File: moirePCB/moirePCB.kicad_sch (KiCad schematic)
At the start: 55 parts, among them J1 USB_C_Receptacle, U1 ESP32-PICO-D4, U1 TLC555xD, U10 TLV73333PDBV, U2 BQ25504, U3 TLV73333PDBV, U4 RFM95W-915S2, U5 CH340E, U7 HDC1080, U8 AP2281-1WG-7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

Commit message: Daughter Board changes from meeting
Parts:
- removed ACC_RAIL_JP1, BATTMEASURE_JP1, LDO_JP1, TEMP_SCL_JP1, TEMP_SDA_JP1, VBAT_OK1: SolderJumper_2_Bridged, Jumper:SolderJumper-2_P1.3mm_Bridged_RoundedPad1.0x1.5mm, symbol Jumper:SolderJumper_2_Bridged
- removed AE1: T1-915M Antenna, Connector_PinHeader_2.54mm:PinHeader_1x01_P2.54mm_Vertical, symbol Device:Antenna
- removed BOOT1, EN1: SW_Push, Button_Switch_SMD:SW_Push_1P1T_XKB_TS-1187A, symbol Switch:SW_Push
- removed BT1: Battery_Cell, Connector_JST:JST_PH_S2B-PH-K_1x02_P2.00mm_Horizontal, symbol Device:Battery_Cell
- removed C1: .1u, Capacitor_SMD:C_0805_2012Metric, symbol Device:C
- removed C2, C6: 12pF/50V, Capacitor_SMD:C_0805_2012Metric, symbol Device:C
- removed C3: .01uF, Capacitor_SMD:C_0805_2012Metric, symbol Device:C
- removed C5: 10u, Capacitor_SMD:C_0805_2012Metric, symbol Device:C
- removed C7: 100nF, Capacitor_SMD:C_0805_2012Metric, symbol Device:C
- removed C_FLTR1: .1uF, Capacitor_SMD:C_0805_2012Metric, symbol Device:C
- removed C_HVR1, C_STOR1: 4.7uF, Capacitor_SMD:C_0805_2012Metric, symbol Device:C
- removed J1: USB_C_Receptacle, Connector_USB:USB_C_Receptacle_HRO_TYPE-C-31-M-12, symbol Connector:USB_C_Receptacle
- removed LDR1: R_Photo 50k-100k, Connector_PinHeader_2.54mm:PinHeader_1x02_P2.54mm_Horizontal, symbol Device:R_Photo
- removed L_BST1: 22uH, Inductor_SMD:L_0805_2012Metric, symbol Device:L
- removed R10: 360k, Resistor_SMD:R_0805_2012Metric, symbol Device:R
- removed R4: 270k, Resistor_SMD:R_0805_2012Metric, symbol Device:R
- removed R6: 5.1k, Resistor_SMD:R_0805_2012Metric, symbol Device:R
- removed R7: 820k, Resistor_SMD:R_0805_2012Metric, symbol Device:R
- removed R_OC+10: 10M, Resistor_SMD:R_0805_2012Metric, symbol Device:R
- removed R_OC_1: 5.76M, Resistor_SMD:R_0805_2012Metric, symbol Device:R
- removed R_OC_2: 4.12M, Resistor_SMD:R_0805_2012Metric, symbol Device:R
- removed R_OK_1: 3.57M, Resistor_SMD:R_0805_2012Metric, symbol Device:R
- removed R_OK_2, R_UV_2: 6.19M, Resistor_SMD:R_0805_2012Metric, symbol Device:R
- removed R_OK_3: .143M, Resistor_SMD:R_0805_2012Metric, symbol Device:R
- removed R_OV_1: 4.42M, Resistor_SMD:R_0805_2012Metric, symbol Device:R
- removed R_OV_2: 5.36M, Resistor_SMD:R_0805_2012Metric, symbol Device:R
- removed R_UV_1: 3.74M, Resistor_SMD:R_0805_2012Metric, symbol Device:R
- removed SC1: Solar_Cell, Connector_PinHeader_2.54mm:PinHeader_1x02_P2.54mm_Horizontal, symbol Device:Solar_Cell
- removed U1: ESP32-PICO-D4, Package_DFN_QFN:QFN-48-1EP_7x7mm_P0.5mm_EP5.3x5.3mm, symbol RF_Module:ESP32-PICO-D4
- removed U10, U3: TLV73333PDBV, Package_TO_SOT_SMD:SOT-23-5, symbol Regulator_Linear:TLV73333PDBV
- removed U2: BQ25504, Package_DFN_QFN:VQFN-16-1EP_3x3mm_P0.5mm_EP1.68x1.68mm, symbol Battery_Management:BQ25504
- removed U4: RFM95W-915S2, RF_Module:HOPERF_RFM9XW_SMD, symbol RF_Module:RFM95W-915S2
- removed U5: CH340E, Package_SO:MSOP-10_3x3mm_P0.5mm, symbol Interface_USB:CH340E
- removed U8, U9: AP2281-1WG-7, Package_TO_SOT_SMD:SOT-23-6, symbol Power_Management:AP2281-1WG-7
- removed USB//OFF1, USB//SOLAR1: SW_DPDT_x2, Button_Switch_SMD:SW_SPDT_PCM12, symbol Switch:SW_DPDT_x2
- removed Y2: 32.768kHz, Crystal:Crystal_SMD_MicroCrystal_CM9V-T1A-2Pin_1.6x1.0mm, symbol Device:Crystal
- added J1, J2: Conn_01x13, Connector_PinHeader_2.54mm:PinHeader_1x13_P2.54mm_Vertical, symbol Connector_Generic:Conn_01x13
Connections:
- net A_VCC: now also J2.1 (Pin_1)
- net GND: now also J1.2 (Pin_2), J2.2 (Pin_2)
- net at U7.1 (SDA): now also J2.5 (Pin_5)
- net at U7.6 (SCL): now also J2.4 (Pin_4)
- new net 5V (USB): J1.1 (Pin_1)
- no-connect marks 16 -> 0
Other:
- note removed: "Accessory Rail"
- note removed: "For internal flash use"
- note removed: "Light Sensor"
- note removed: "USB/UART Converter"
- note removed: "external RTC crystal"
- note removed: "reset button"
- moved on the sheet: C1, C2, FREQOUT_JP1, R1, R2, U1, U7

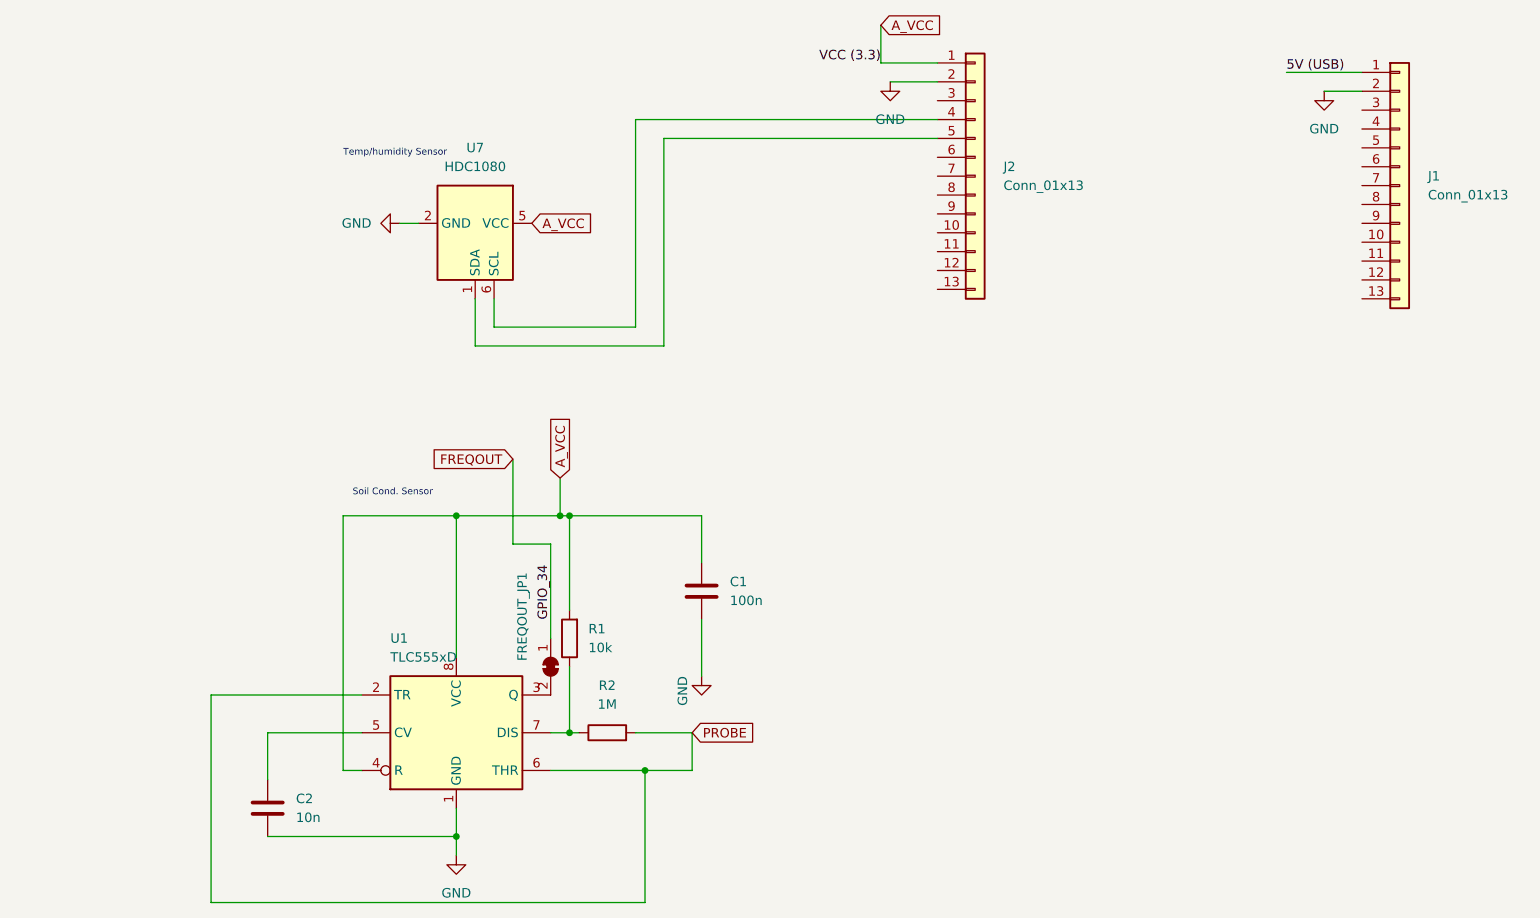
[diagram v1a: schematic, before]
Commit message: Daughter board prototype 1.0.0
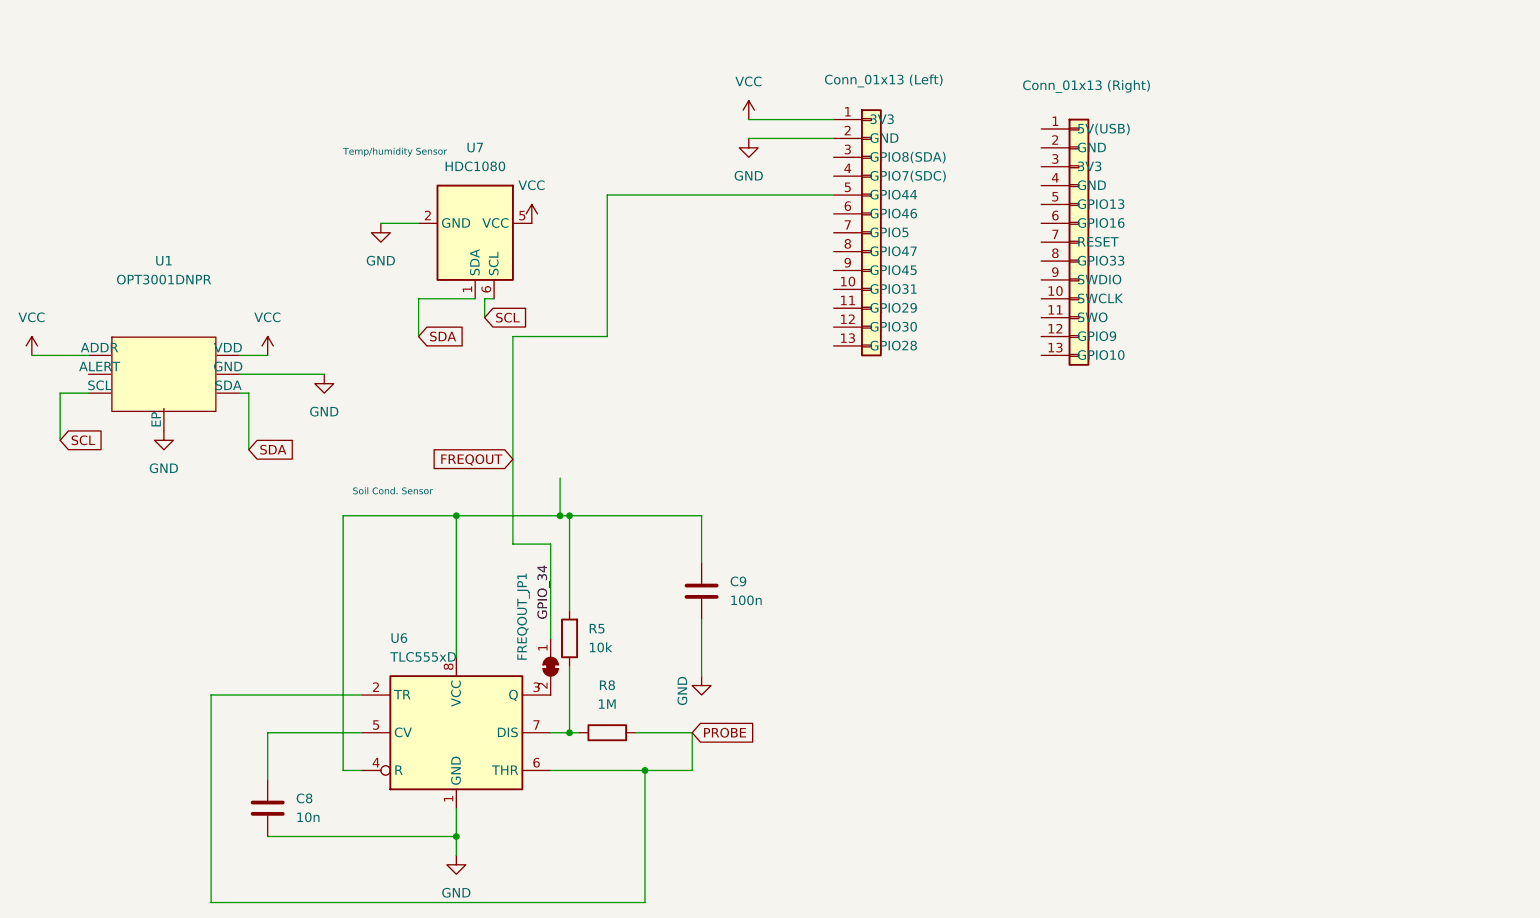
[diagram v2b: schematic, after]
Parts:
- added U1: OPT3001DNPR, OPT3001.pretty:OPT3001, symbol OptTI:OPT3001
- J1: value Conn_01x13 -> Conn_01x13 (Right); footprint Connector_PinHeader_2.54mm:PinHeader_1x13_P2.54mm_Vertical -> Connector_PinSocket_2.54mm:PinSocket_1x13_P2.54mm_Vertical
- J2: value Conn_01x13 -> Conn_01x13 (Left); footprint Connector_PinHeader_2.54mm:PinHeader_1x13_P2.54mm_Vertical -> Connector_PinSocket_2.54mm:PinSocket_1x13_P2.54mm_Vertical
- renumbered C2 to C8, C1 to C9, R1 to R5, R2 to R8, U1 to U6
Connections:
- net FREQOUT: now also J2.5 (GPIO44)
- net GND: now also U1.5 (GND), U1.7 (EP); no longer J1.2 (Pin_2)
- net at J2.4 (GPIO7(SDC)): no longer U7.6 (SCL)
- net SDA: now reaches U7.1 (SDA)
- net SDA: now also U1.4 (SDA); no longer J2.5 (Pin_5)
- net 5V (USB): no longer names the net of J1.1 (5V(USB))
- net A_VCC: no longer names the net of C9.1, R5.2, U6.4 (R), U6.8 (VCC)
- net A_VCC: no longer J2.1 (Pin_1), U7.5 (VCC)
- new net SCL: U1.3 (SCL), U7.6 (SCL)
- new net VCC: J2.1 (3V3), U1.1 (ADDR), U1.6 (VDD), U7.5 (VCC)

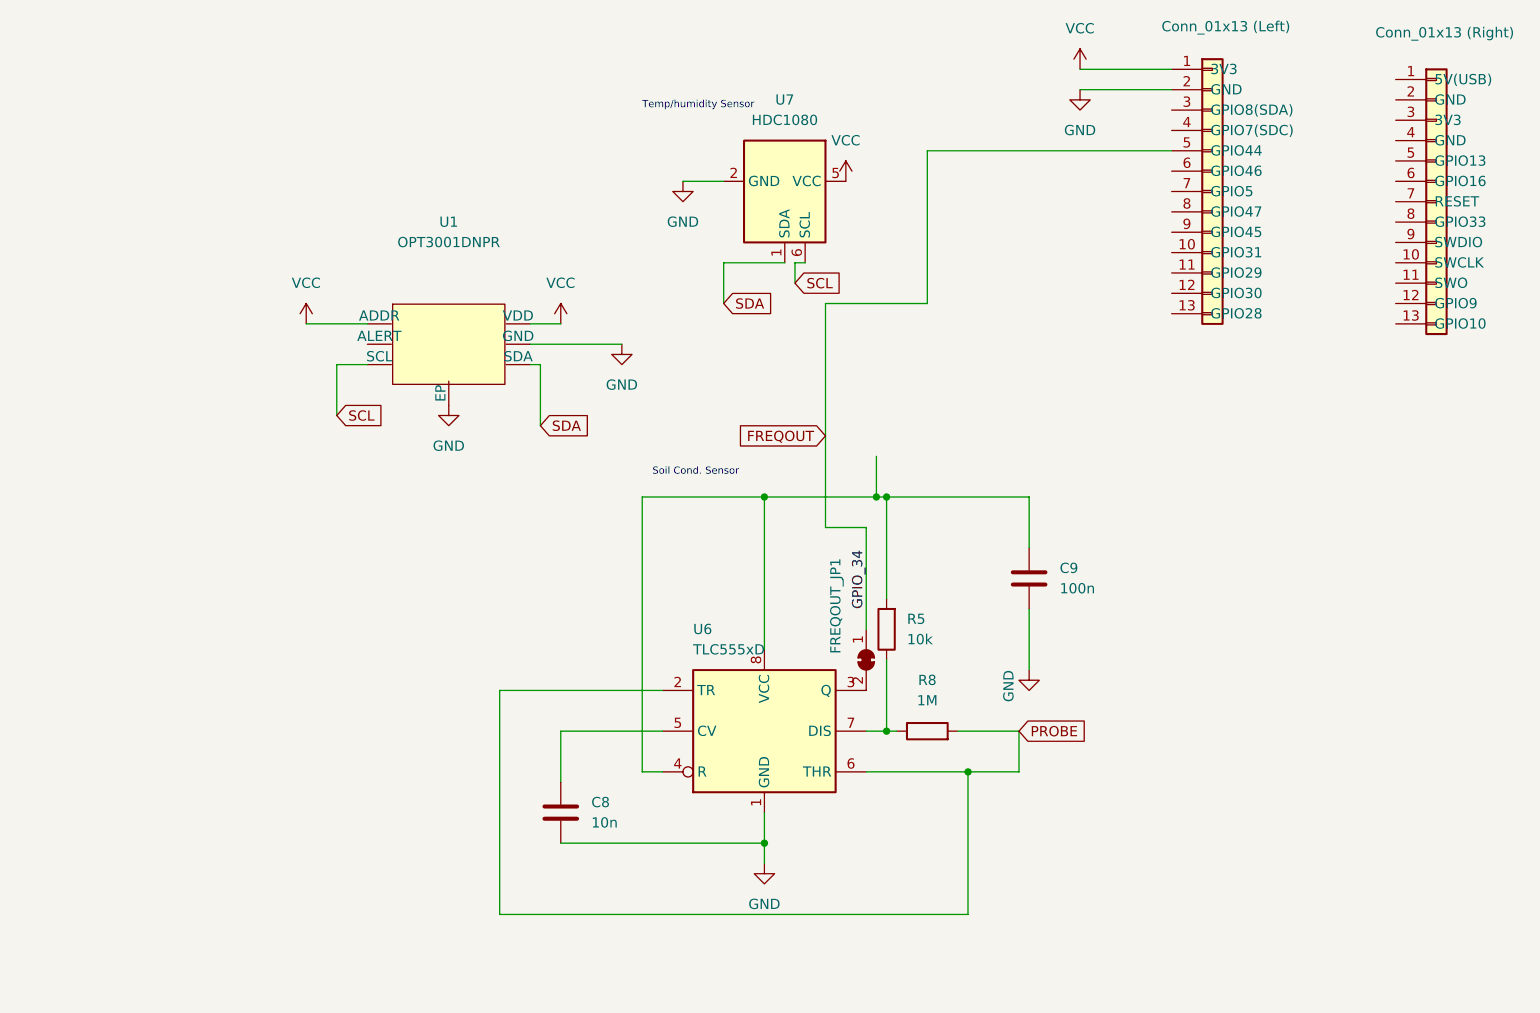
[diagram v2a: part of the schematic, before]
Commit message: Daughter board prototype 1.0.0
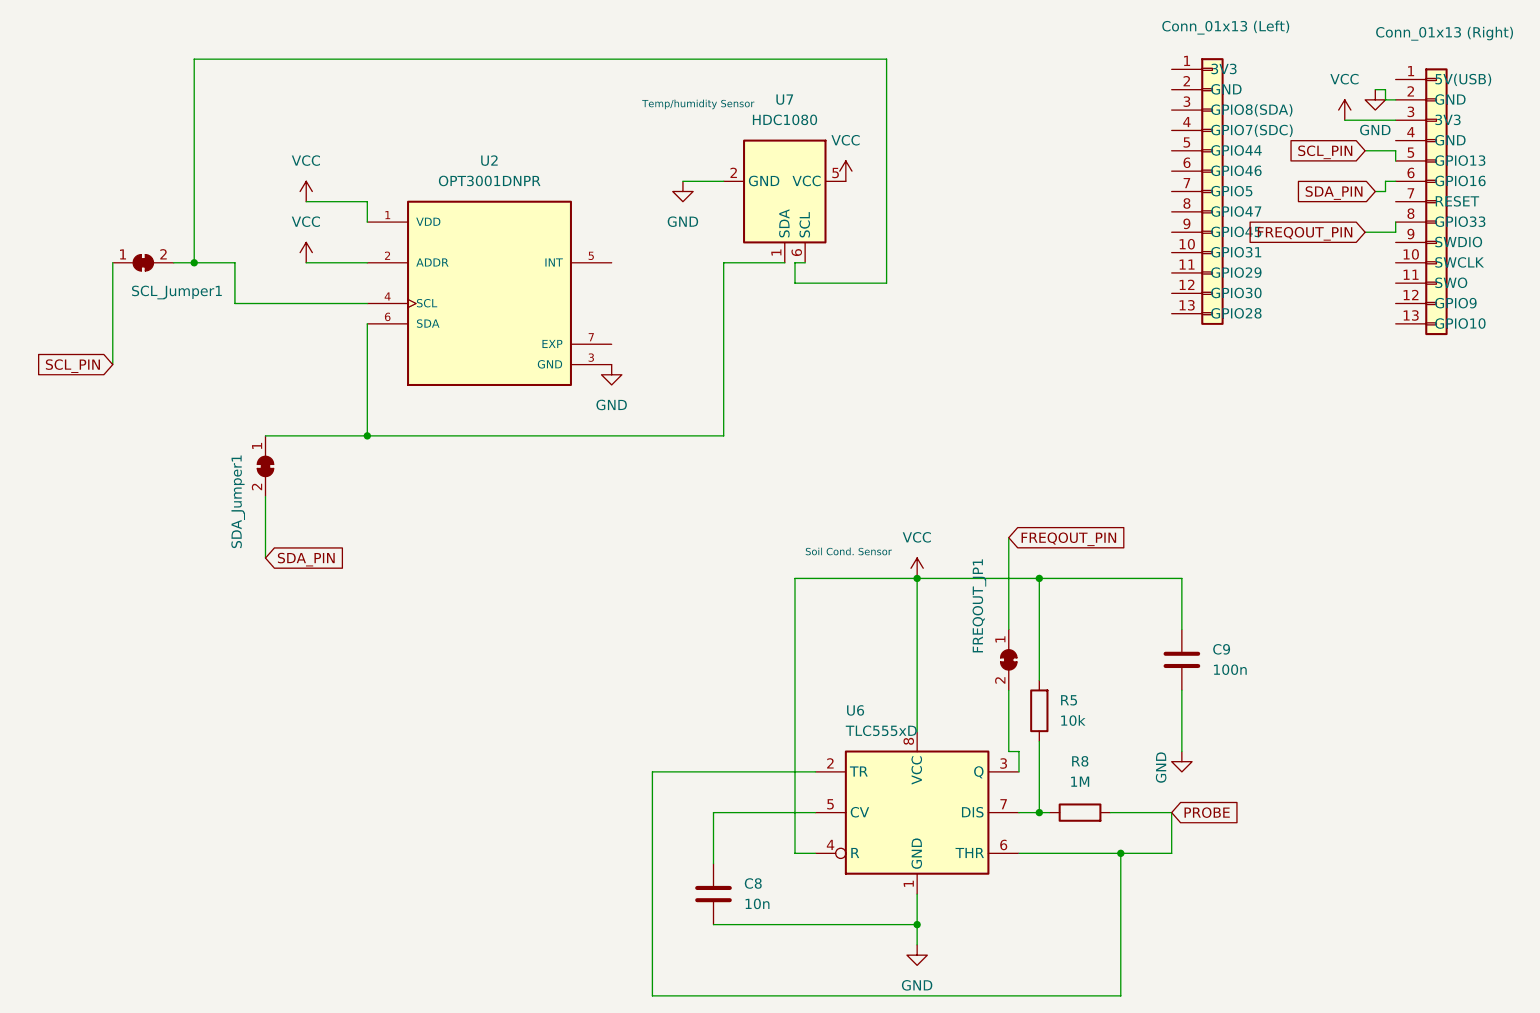
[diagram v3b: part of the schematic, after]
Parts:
- removed U1: OPT3001DNPR, OPT3001.pretty:OPT3001, symbol OptTI:OPT3001
- added SCL_Jumper1, SDA_Jumper1: SolderJumper_2_Bridged, Jumper:SolderJumper-2_P1.3mm_Bridged_RoundedPad1.0x1.5mm, symbol Jumper:SolderJumper_2_Bridged
- added U2: OPT3001DNPR, OPT3001DNPR:SON65P200X200X65-7N, symbol OPT3001DNPR:OPT3001DNPR
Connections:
- net GND: now also J1.2 (GND), U2.3 (GND); no longer J2.2 (GND)
- net VCC: now also C9.1, J1.3 (3V3), R5.2, U6.4 (R), U6.8 (VCC), U2.1 (VDD), U2.2 (ADDR); no longer J2.1 (3V3)
- net SCL_PIN: now reaches J1.5 (GPIO13)
- net SCL_PIN: now also SCL_Jumper1.1 (A)
- net SDA_PIN: now reaches J1.6 (GPIO16)
- net SDA_PIN: now also SDA_Jumper1.2 (B)
- net FREQOUT_PIN: now reaches J1.8 (GPIO33)
- net FREQOUT_PIN: now also FREQOUT_JP1.1 (A)
- net FREQOUT: no longer names the net of J2.5 (GPIO44)
- net FREQOUT: no longer FREQOUT_JP1.1 (A)
- net SCL: no longer names the net of U7.6 (SCL)
- net SCL: now also SCL_Jumper1.2 (B), U2.4 (SCL)
- net SDA: no longer names the net of U7.1 (SDA)
- net SDA: now also SDA_Jumper1.1 (A), U2.6 (SDA)
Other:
- moved on the sheet: C8, C9, FREQOUT_JP1, R5, R8, U6
